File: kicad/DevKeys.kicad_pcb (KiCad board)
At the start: 2 copper layers, 22 parts, among them SW1 SWITCH_PUSH, SW10 SWITCH_PUSH, SW2 SWITCH_PUSH, SW3 SWITCH_PUSH, SW4 SWITCH_PUSH, SW5 SWITCH_PUSH, SW6 SWITCH_PUSH, SW7 SWITCH_PUSH, SW8 SWITCH_PUSH, SW9 SWITCH_PUSH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

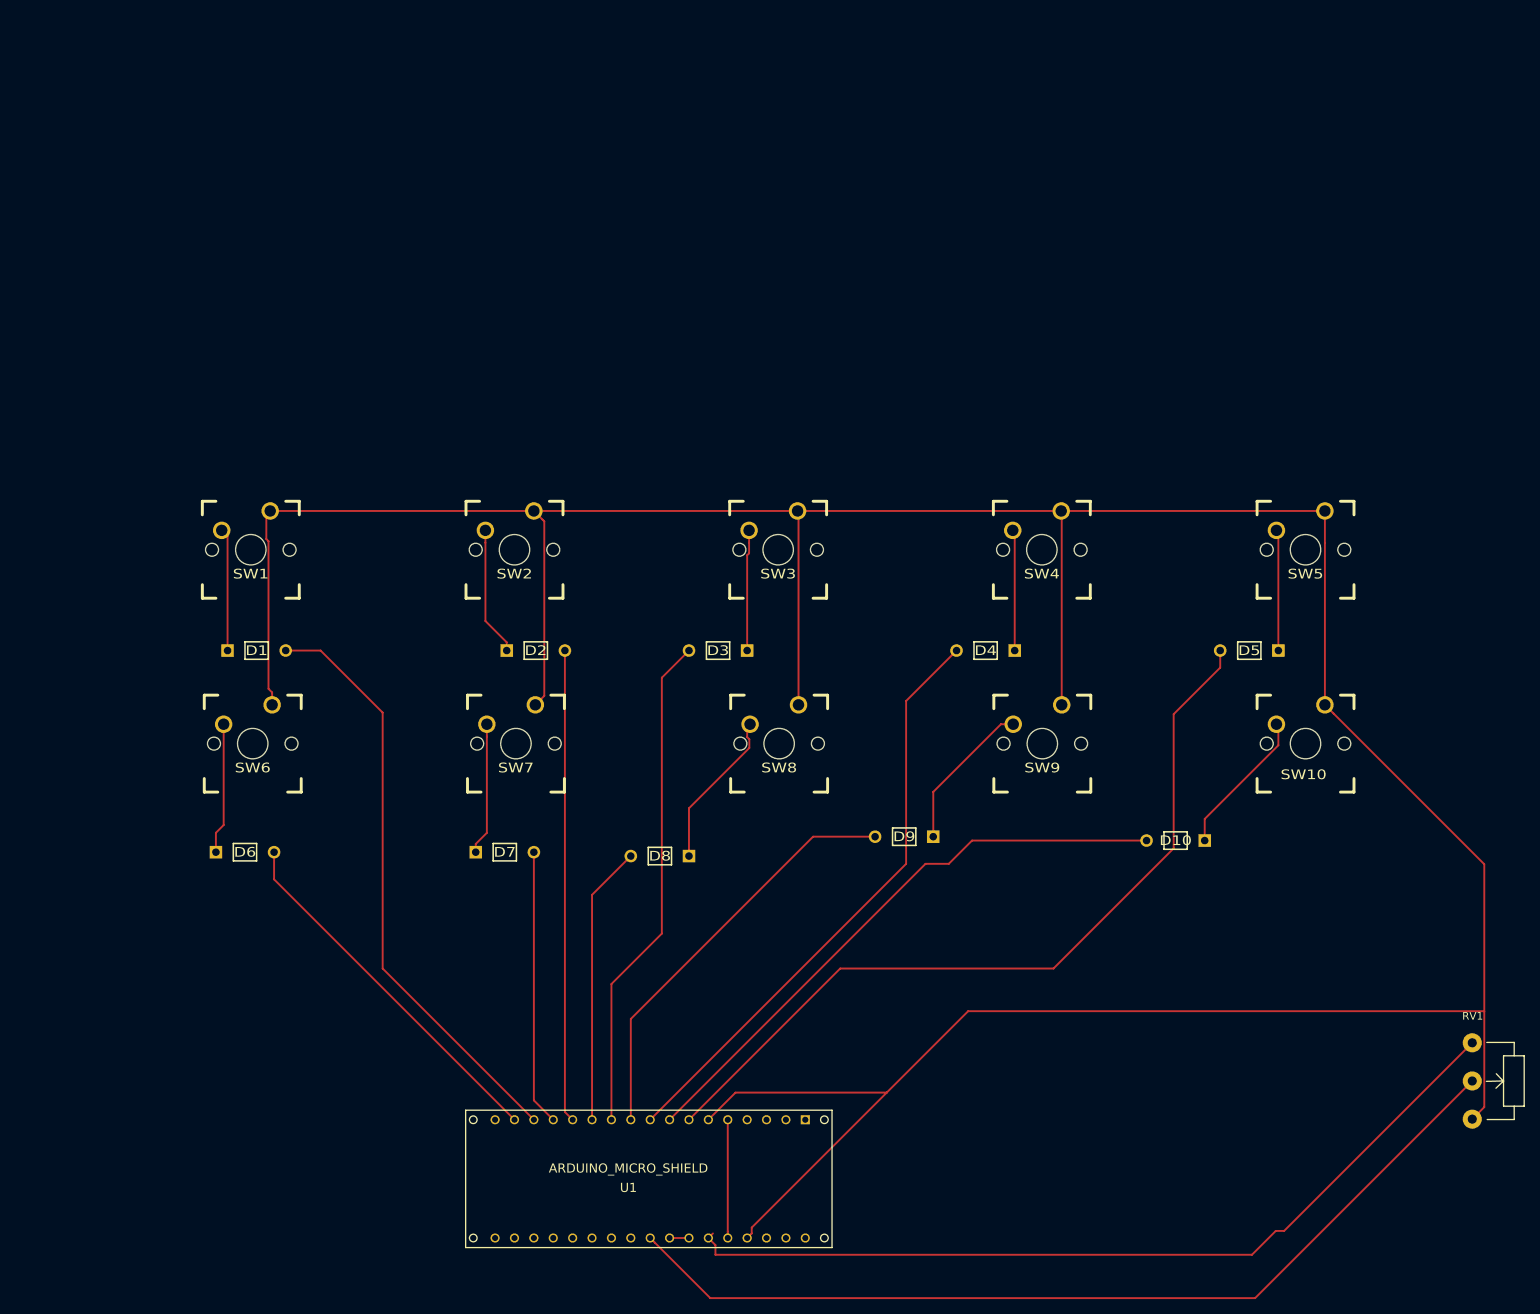
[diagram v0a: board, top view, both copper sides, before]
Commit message: dioden vor den Tasten entfernt
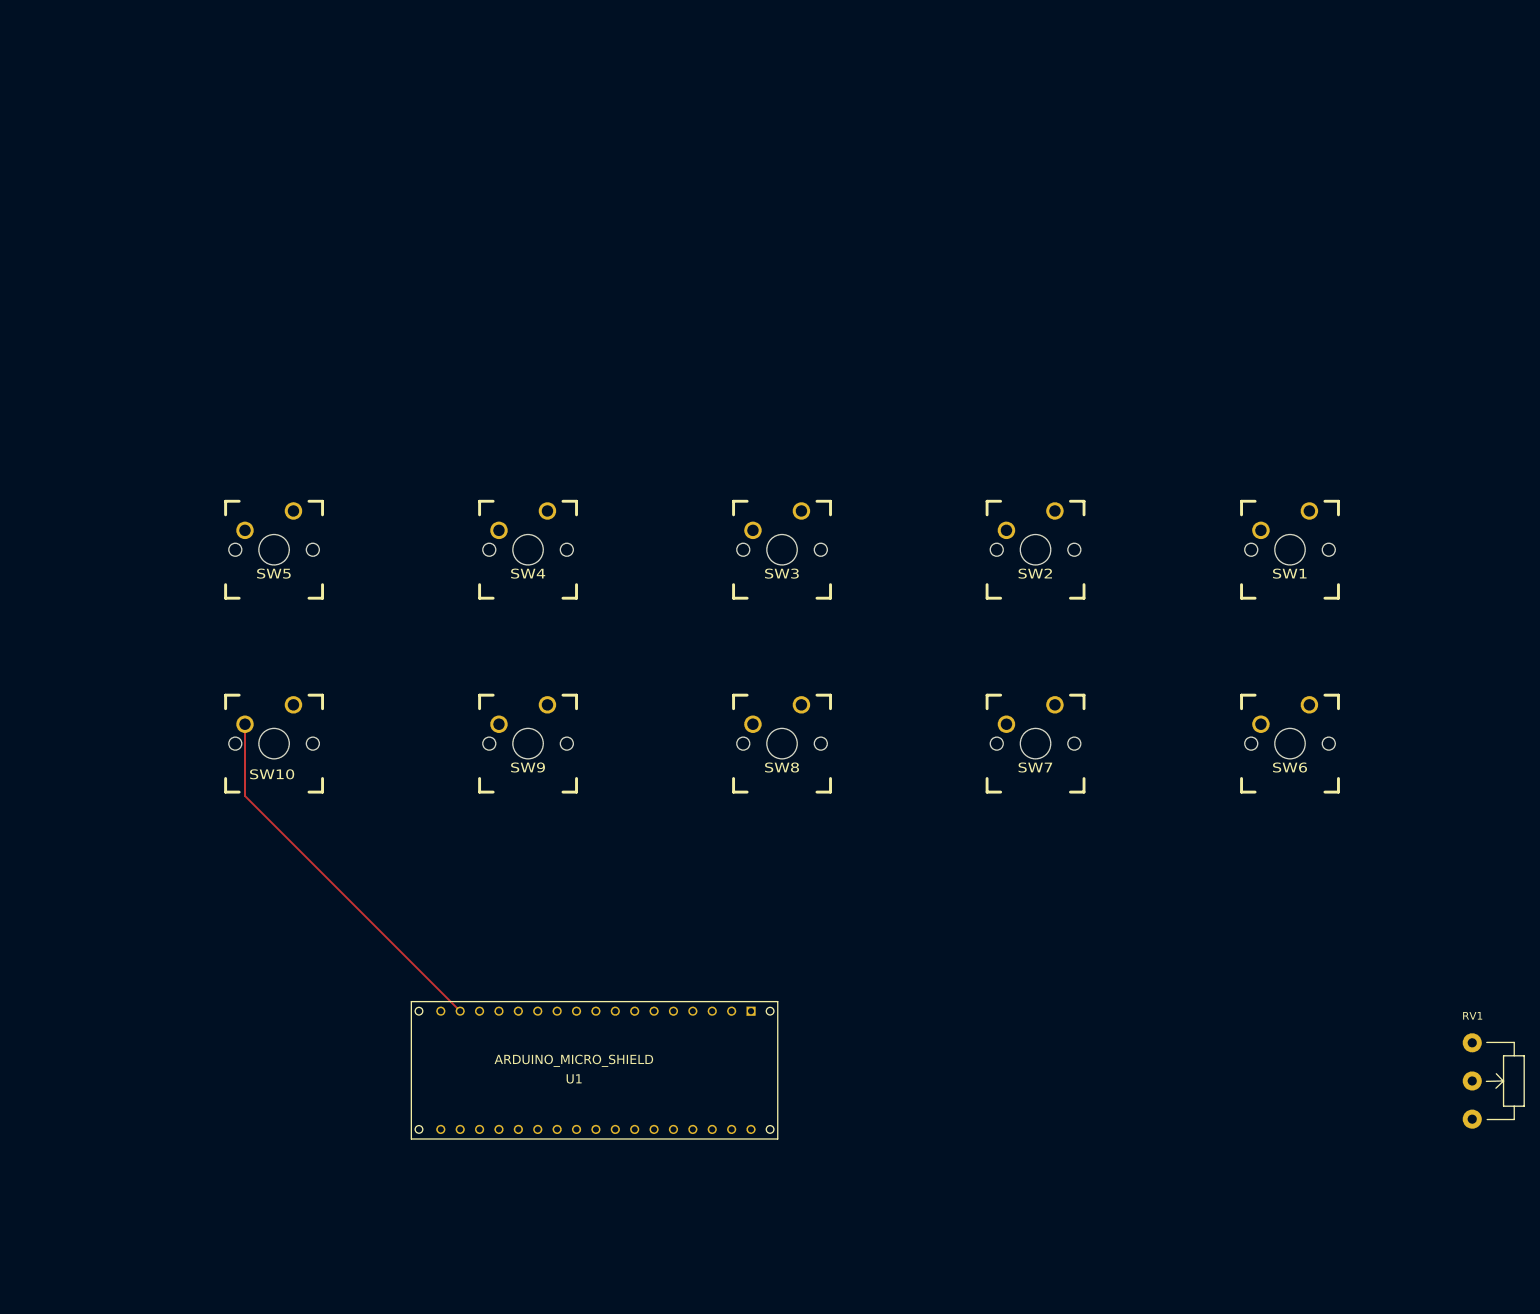
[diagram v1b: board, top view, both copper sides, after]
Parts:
- removed D1, D10, D2, D3, D4, D5, D6, D7, D8, D9: DIODE, footprints:DIODE
- moved SW1 136.1 mm to (169.2, 70.1)
- moved SW6 135.9 mm to (169.2, 95.5)
- moved SW10 135.1 mm to (36.1, 95.5)
- moved SW5 135.1 mm to (36.1, 70.1)
- moved SW2 68.3 mm to (135.8, 70.1)
- moved SW7 68.1 mm to (135.8, 95.5)
- moved SW9 67.4 mm to (69.3, 95.5)
- moved SW4 67.3 mm to (69.3, 70.1)
- moved U1 15.9 mm to (102.1, 129.3)
- moved SW3 0.51 mm to (102.6, 70.1)
- moved SW8 0.38 mm to (102.6, 95.5)
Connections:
- SW1 pad 2: Net-(D1-Pad2) -> Net-(SW1-Pad2)
- SW10 pad 2: Net-(D10-Pad2) -> Net-(SW10-Pad2)
- SW2 pad 2: Net-(D2-Pad2) -> Net-(SW2-Pad2)
- SW3 pad 2: Net-(D3-Pad2) -> Net-(SW3-Pad2)
- SW4 pad 2: Net-(D4-Pad2) -> Net-(SW4-Pad2)
- SW5 pad 2: Net-(D5-Pad2) -> Net-(SW5-Pad2)
- SW6 pad 2: Net-(D6-Pad2) -> Net-(SW6-Pad2)
- SW7 pad 2: Net-(D7-Pad2) -> Net-(SW7-Pad2)
- SW8 pad 2: Net-(D8-Pad2) -> Net-(SW8-Pad2)
- SW9 pad 2: Net-(D9-Pad2) -> Net-(SW9-Pad2)
- U1 pad 10: Net-(D1-Pad1) -> Net-(SW5-Pad2)
- U1 pad 11: Net-(D6-Pad1) -> Net-(SW10-Pad2)
- U1 pad 12: Net-(U1-Pad12) -> (no net)
- U1 pad 13: Net-(U1-Pad13) -> (no net)
- U1 pad 2: Net-(D5-Pad1) -> Net-(SW6-Pad2)
- U1 pad 3: Net-(D10-Pad1) -> Net-(SW1-Pad2)
- U1 pad 3.3V: Net-(U1-Pad3.3V) -> (no net)
- U1 pad 4: Net-(D4-Pad1) -> Net-(SW7-Pad2)
- U1 pad 5: Net-(D9-Pad1) -> Net-(SW2-Pad2)
- U1 pad 6: Net-(D3-Pad1) -> Net-(SW8-Pad2)
- U1 pad 7: Net-(D8-Pad1) -> Net-(SW3-Pad2)
- U1 pad 8: Net-(D2-Pad1) -> Net-(SW4-Pad2)
- U1 pad 9: Net-(D7-Pad1) -> Net-(SW9-Pad2)
- U1 pad A0: Net-(U1-PadA0) -> (no net)
- U1 pad A1: Net-(U1-PadA1) -> (no net)
- U1 pad A2: Net-(U1-PadA2) -> (no net)
- U1 pad A3: Net-(U1-PadA3) -> (no net)
- U1 pad A4: Net-(U1-PadA4) -> (no net)
- U1 pad AREF: Net-(U1-PadAREF) -> (no net)
- U1 pad MI: Net-(U1-PadMI) -> (no net)
- U1 pad MO: Net-(U1-PadMO) -> (no net)
- U1 pad RX: Net-(U1-PadRX) -> (no net)
- U1 pad SCK: Net-(U1-PadSCK) -> (no net)
- U1 pad SS: Net-(U1-PadSS) -> (no net)
- U1 pad TX: Net-(U1-PadTX) -> (no net)
- U1 pad VI: Net-(U1-PadVI) -> (no net)
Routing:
- net Net-(RV1-Pad3): track 464.6 -> 0.00 mm
- net Net-(RV1-Pad2): track 122.7 -> 0.00 mm
- net Net-(RV1-Pad1): track 114.1 -> 0.00 mm
- net Net-(D5-Pad1): track 106.7 -> 0.00 mm
- net Net-(D4-Pad1): track 78.1 -> 0.00 mm
- net Net-(D10-Pad1): track 77.6 -> 0.00 mm
- net Net-(D1-Pad1): track 77.6 -> 0.00 mm
- net Net-(D3-Pad1): track 65.7 -> 0.00 mm
- net Net-(D2-Pad1): track 61.9 -> 0.00 mm
- net Net-(D9-Pad1): track 55.1 -> 0.00 mm
- net Net-(SW10-Pad2): track 0.00 -> 49.3 mm
- net Net-(D6-Pad1): track 48.1 -> 0.00 mm
- net Net-(D8-Pad1): track 36.6 -> 0.00 mm
- net Net-(D7-Pad1): track 36.1 -> 0.00 mm
- net Net-(D8-Pad2): track 20.8 -> 0.00 mm
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
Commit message: finished layout for first prototype pcb
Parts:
- SW1, SW10, SW2, SW3, SW4, SW5, SW6, SW7, SW8, SW9: footprint footprints:CHERRY_PCB_150H -> footprints:CHERRY_PCB_100H
- moved RV1 81.7 mm to (113.8, 114.9)
- moved SW1 55.1 mm to (114.3, 75.7)
- moved SW6 54.9 mm to (114.3, 95.5)
- moved SW2 41.5 mm to (94.7, 75.7)
- moved SW7 41.1 mm to (94.7, 95.5)
- moved U1 30.9 mm to (76.1, 112.5)
- moved SW3 28.0 mm to (75.2, 75.7)
- moved SW8 27.4 mm to (75.2, 95.5)
- moved SW4 14.8 mm to (55.6, 75.7)
- moved SW9 13.7 mm to (55.6, 95.5)
- moved SW5 5.59 mm to (36.1, 75.7)
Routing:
- net Net-(RV1-Pad3): track 0.00 -> 428.1 mm
- net Net-(SW1-Pad2): track 0.00 -> 84.7 mm
- net Net-(RV1-Pad2): track 0.00 -> 68.7 mm
- net Net-(SW2-Pad2): track 0.00 -> 67.7 mm
- net Net-(SW4-Pad2): track 0.00 -> 65.7 mm
- net Net-(RV1-Pad1): track 0.00 -> 61.8 mm
- net Net-(SW6-Pad2): track 0.00 -> 61.8 mm
- net Net-(SW3-Pad2): track 0.00 -> 55.1 mm
- net Net-(SW5-Pad2): track 0.00 -> 54.3 mm
- net Net-(SW7-Pad2): track 0.00 -> 47.2 mm
- net Net-(SW8-Pad2): track 0.00 -> 36.7 mm
- net Net-(SW9-Pad2): track 0.00 -> 26.9 mm
- net Net-(SW10-Pad2): track 49.3 -> 25.6 mm
- net Net-(U1-PadRST): track 0.00 -> 16.0 mm
- net Net-(U1-PadNC): track 0.00 -> 2.54 mm
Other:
- net class Default: clearance 0.2 -> 0.8; trace_width 0.25 -> 0.8
- rule trace_clearance: 0.2 -> 0.8

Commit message: neues Platinen-Layout
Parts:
- removed RV1: POT, Potentiometers:Potentiometer_WirePads
- removed SW1, SW10, SW2, SW3, SW4, SW5, SW6, SW7, SW8, SW9: SWITCH_PUSH, footprints:CHERRY_PCB_100H
- removed U1: ARDUINO_MICRO_SHIELD, arduino_micro_shield:ARDUINO_MICRO_SHIELD
- added J1: RaspberryPiZeroW, Pin_Headers:Pin_Header_Straight_2x20_Pitch2.54mm, F.Cu at (5.84, 5.84)
- added J2: Display, Socket_Strips:Socket_Strip_Straight_1x04_Pitch2.54mm, F.Cu at (34.3, 22.4)
- added S1: KeyStart, mx1a:MX1A, F.Cu at (55.6, 9.65)
- added S10: KeyEvaluateSelection, mx1a:MX1A, F.Cu at (124.2, 55.4)
- added S2: KeyStop, mx1a:MX1A, F.Cu at (78.5, 9.65)
- added S3: KeySelect, mx1a:MX1A, F.Cu at (124.2, 9.65)
- added S4: KeyStepOver, mx1a:MX1A, F.Cu at (55.6, 32.5)
- added S5: KeyStepInto, mx1a:MX1A, F.Cu at (78.5, 32.5)
- added S6: KeyStepOut, mx1a:MX1A, F.Cu at (101.3, 32.5)
- added S7: KeyRunToCursor, mx1a:MX1A, F.Cu at (55.6, 55.4)
- added S8: KeyRunSection, mx1a:MX1A, F.Cu at (78.5, 55.4)
- added S9: KeyRunAndAdvance, mx1a:MX1A, F.Cu at (101.3, 55.4)
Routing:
- net Net-(RV1-Pad3): track 428.1 -> 0.00 mm
- net Net-(J1-Pad30): track 0.00 -> 139.7 mm
- net Net-(J1-Pad40): track 0.00 -> 136.5 mm
- net Net-(J1-Pad12): track 0.00 -> 131.3 mm
- net Net-(J1-Pad6): track 0.00 -> 122.7 mm
- net Net-(J1-Pad38): track 0.00 -> 111.9 mm
- net Net-(J1-Pad20): track 0.00 -> 110.6 mm
- net Net-(J1-Pad26): track 0.00 -> 109.4 mm
- net Net-(J1-Pad36): track 0.00 -> 87.9 mm
- net Net-(J1-Pad24): track 0.00 -> 85.1 mm
- net Net-(SW1-Pad2): track 84.7 -> 0.00 mm
- net Net-(J1-Pad10): track 0.00 -> 83.9 mm
- net Net-(RV1-Pad2): track 68.7 -> 0.00 mm
- net Net-(SW2-Pad2): track 67.7 -> 0.00 mm
- net Net-(SW4-Pad2): track 65.7 -> 0.00 mm
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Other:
- net class Default: clearance 0.8 -> 0.2; trace_width 0.8 -> 0.25
- rule trace_clearance: 0.8 -> 0.2
